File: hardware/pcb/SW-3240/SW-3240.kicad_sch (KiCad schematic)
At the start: 39 parts, among them J1 MIC, J10 CH_D, J2 LINE IN, J3 ESPFlash, J4 JTAG, J5 I2C, J6 FP_IO, J7 CH_A, J8 CH_B, J9 CH_C, SW1 RESET, SW2 BOOT, U1 SW-32MA, U2 MCP4728, U3 ESP32-WROOM-32D, U4 Channel A, U5 Channel B, U6 Channel C, U7 Channel D

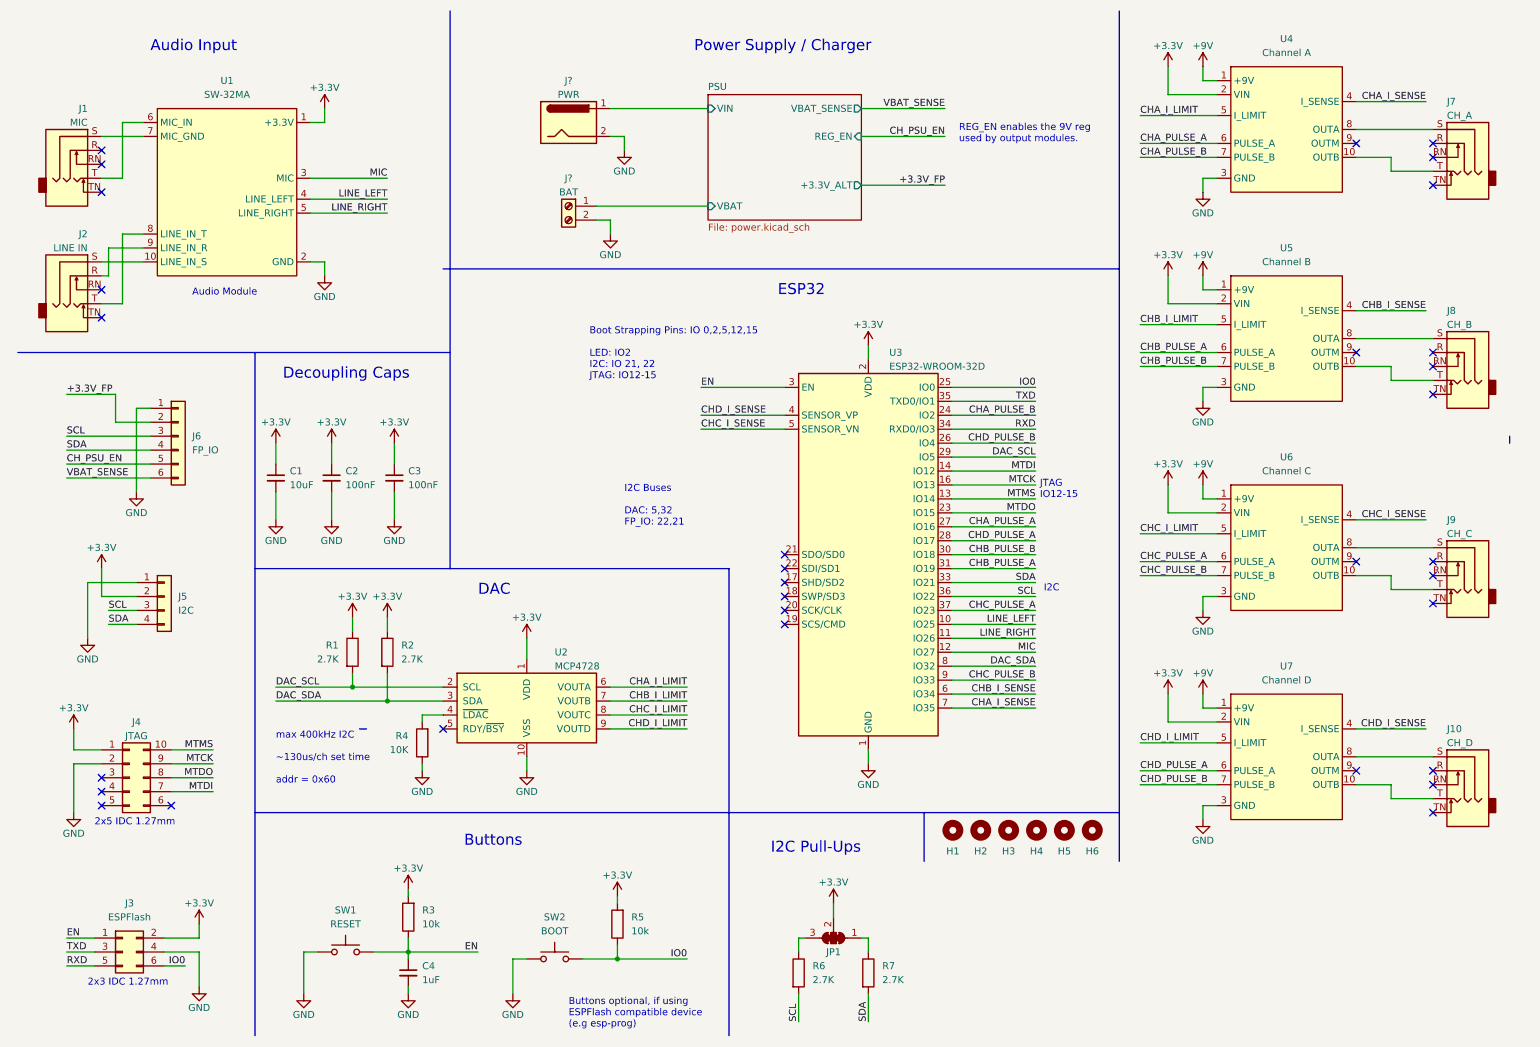
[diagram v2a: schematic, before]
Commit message: fix footprint pin mismatch
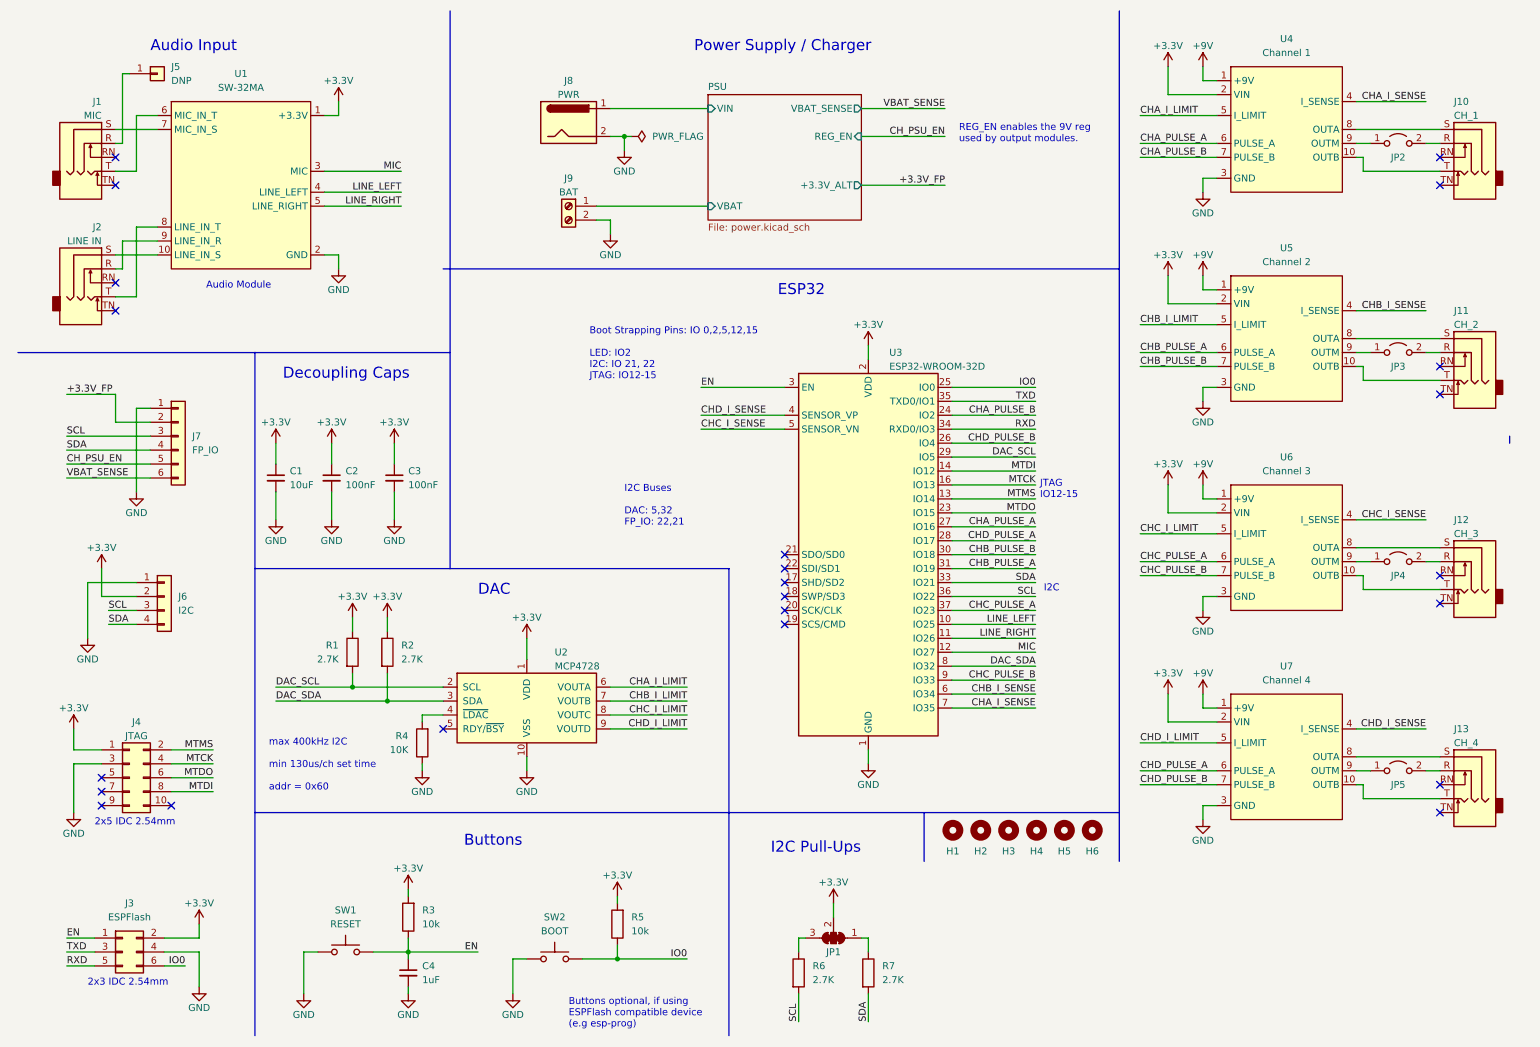
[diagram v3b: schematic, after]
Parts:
- added J5: DNP, Connector_PinHeader_2.54mm:PinHeader_1x01_P2.54mm_Vertical, symbol Connector_Generic:Conn_01x01
- added JP2, JP3, JP4, JP5: Jumper_2_Open, Connector_PinHeader_2.54mm:PinHeader_2x01_P2.54mm_Vertical, symbol Jumper:Jumper_2_Open
- J10: renamed from J7; value CH_A -> CH_1
- J11: renamed from J8; value CH_B -> CH_2
- J12: renamed from J9; value CH_C -> CH_3
- J13: renamed from J10; value CH_D -> CH_4
- J3: footprint Connector_PinHeader_1.27mm:PinHeader_2x03_P1.27mm_Vertical -> Connector_PinHeader_2.54mm:PinHeader_2x03_P2.54mm_Vertical
- J4: footprint Connector_PinHeader_1.27mm:PinHeader_2x05_P1.27mm_Vertical -> Connector_PinHeader_2.54mm:PinHeader_2x05_P2.54mm_Vertical; symbol Connector_Generic:Conn_02x05_Counter_Clockwise -> Connector_Generic:Conn_02x05_Odd_Even
- U4: value Channel A -> Channel 1
- U5: value Channel B -> Channel 2
- U6: value Channel C -> Channel 3
- U7: value Channel D -> Channel 4
- gave numbers to parts that had none: 2
- renumbered J5 to J6, J6 to J7
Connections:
- net GND: now also J4.3 (Pin_3); no longer J4.2 (Pin_2)
- net MTCK: now also J4.4 (Pin_4); no longer J4.9 (Pin_9)
- net MTDI: now also J4.8 (Pin_8); no longer J4.7 (Pin_7)
- net MTDO: now also J4.6 (Pin_6); no longer J4.8 (Pin_8)
- net MTMS: now also J4.2 (Pin_2); no longer J4.10 (Pin_10)
- net at J10.R: now also JP2.2 (B)
- net at J11.R: now also JP3.2 (B)
- net at U5.9 (OUTM): now also JP3.1 (A)
- net at J1.R: now also J5.1 (Pin_1)
- net at J12.R: now also JP4.2 (B)
- net at U7.9 (OUTM): now also JP5.1 (A)
- net at J13.R: now also JP5.2 (B)
- net at U6.9 (OUTM): now also JP4.1 (A)
- net at U4.9 (OUTM): now also JP2.1 (A)
- no-connect marks 32 -> 23
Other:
- note added: "2x3 IDC 2.54mm"
- note added: "2x5 IDC 2.54mm"
- note added: "max 400kHz I2C min 130us/ch set time addr = 0x60"
- note removed: "2x3 IDC 1.27mm"
- note removed: "2x5 IDC 1.27mm"
- note removed: "max 400kHz I2C ~130us/ch set time addr = 0x60"
- moved on the sheet: J1, J10, J11, J12, J13, J2, U1

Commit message: many changes
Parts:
- removed SW1: RESET, Button_Switch_SMD:SW_Push_SPST_NO_Alps_SKRK, symbol Switch:SW_Push
- removed SW2: BOOT, Button_Switch_SMD:SW_Push_SPST_NO_Alps_SKRK, symbol Switch:SW_Push
- added C1: 10uF, Capacitor_SMD:C_0603_1608Metric, symbol Device:C_Small
- added C3: 100uF, Capacitor_SMD:C_0603_1608Metric, symbol Device:C_Small
- added J1: AUX_MIC_IN, Connector_PinHeader_2.54mm:PinHeader_1x02_P2.54mm_Vertical, symbol Connector_Generic:Conn_01x02
- added J11: RESET/FLASH, Connector_PinHeader_2.54mm:PinHeader_2x02_P2.54mm_Vertical, symbol Connector_Generic:Conn_02x02_Odd_Even
- added J2: AUX_LINE_IN, Connector_PinHeader_2.54mm:PinHeader_1x04_P2.54mm_Vertical, symbol Connector_Generic:Conn_01x04
- added J7: FP_5V, Connector_JST:JST_XH_B2B-XH-A_1x02_P2.50mm_Vertical, symbol Connector_Generic:Conn_01x02
- J10: renamed from J7; footprint (none) -> Connector_JST:JST_XH_B6B-XH-A_1x06_P2.50mm_Vertical
- J9: renamed from J5; value DNP -> MIC_IN_R
- JP2, JP3, JP4, JP5: value Jumper_2_Open -> TRI_PHASE
- renumbered C1 to C5, C3 to C6, J8 to J12, J9 to J13, J10 to J14, J11 to J15, J12 to J16, J13 to J17, J1 to J3, J2 to J4, J4 to J5, J3 to J6, J6 to J8, R4 to R3, R5 to R4, R3 to R5
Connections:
- net +3V3: now also C1.1, C3.1
- net CHA_PULSE_A: now also U3.26 (IO4); no longer U3.27 (IO16)
- net CHD_PULSE_B: now also U3.27 (IO16); no longer U3.26 (IO4)
- net EN: now also J11.2 (Pin_2)
- net GND: now also C1.2, C3.2, J11.1 (Pin_1), J11.3 (Pin_3), J7.2 (Pin_2)
- net IO0: now also J11.4 (Pin_4)
- net LINE_LEFT: now also U3.11 (IO26); no longer U3.10 (IO25)
- net LINE_RIGHT: now also U3.10 (IO25); no longer U3.11 (IO26)
- net at J3.S, U1.7 (MIC_IN_S): now also J1.1 (Pin_1)
- net at J3.TN: now also J1.2 (Pin_2)
- net at J4.S, U1.10 (LINE_IN_S): now also J2.2 (Pin_2), J2.3 (Pin_3)
- net at J4.RN: now also J2.4 (Pin_4)
- net at J4.TN: now also J2.1 (Pin_1)
- new net +5V: J7.1 (Pin_1)
- no-connect marks 23 -> 20
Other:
- note added: "Boot Strapping Pins (Pull-up/down): - 0 PU - 2 PD - 5 PU - 12 PD - 15 PU Front Panel I2C: IO 21, 22 DAC I2C: IO 32,5 JTAG: IO12-15"
- note added: "DNP"
- note added: "Manual Reset/Boot"
- note added: "Output Channels"
- note added: "Pin header for manually resetting/flashing the ESP-32. Not needed, if using an ESPFlash compatible device (e.g esp-prog)."
- note added: "Separate 1A 3.3V output used for front panel"
- note removed: "Boot Strapping Pins: IO 0,2,5,12,15 LED: IO2 I2C: IO 21, 22 JTAG: IO12-15"
- note removed: "Buttons"
- note removed: "Buttons optional, if using ESPFlash compatible device (e.g esp-prog)"
- note removed: "Decoupling Caps"
- note removed: "I2C Buses DAC: 5,32 FP_IO: 22,21"
- moved on the sheet: C2, C4, C5, C6, J10, J3, J4, J5, J6, J8, J9, R4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

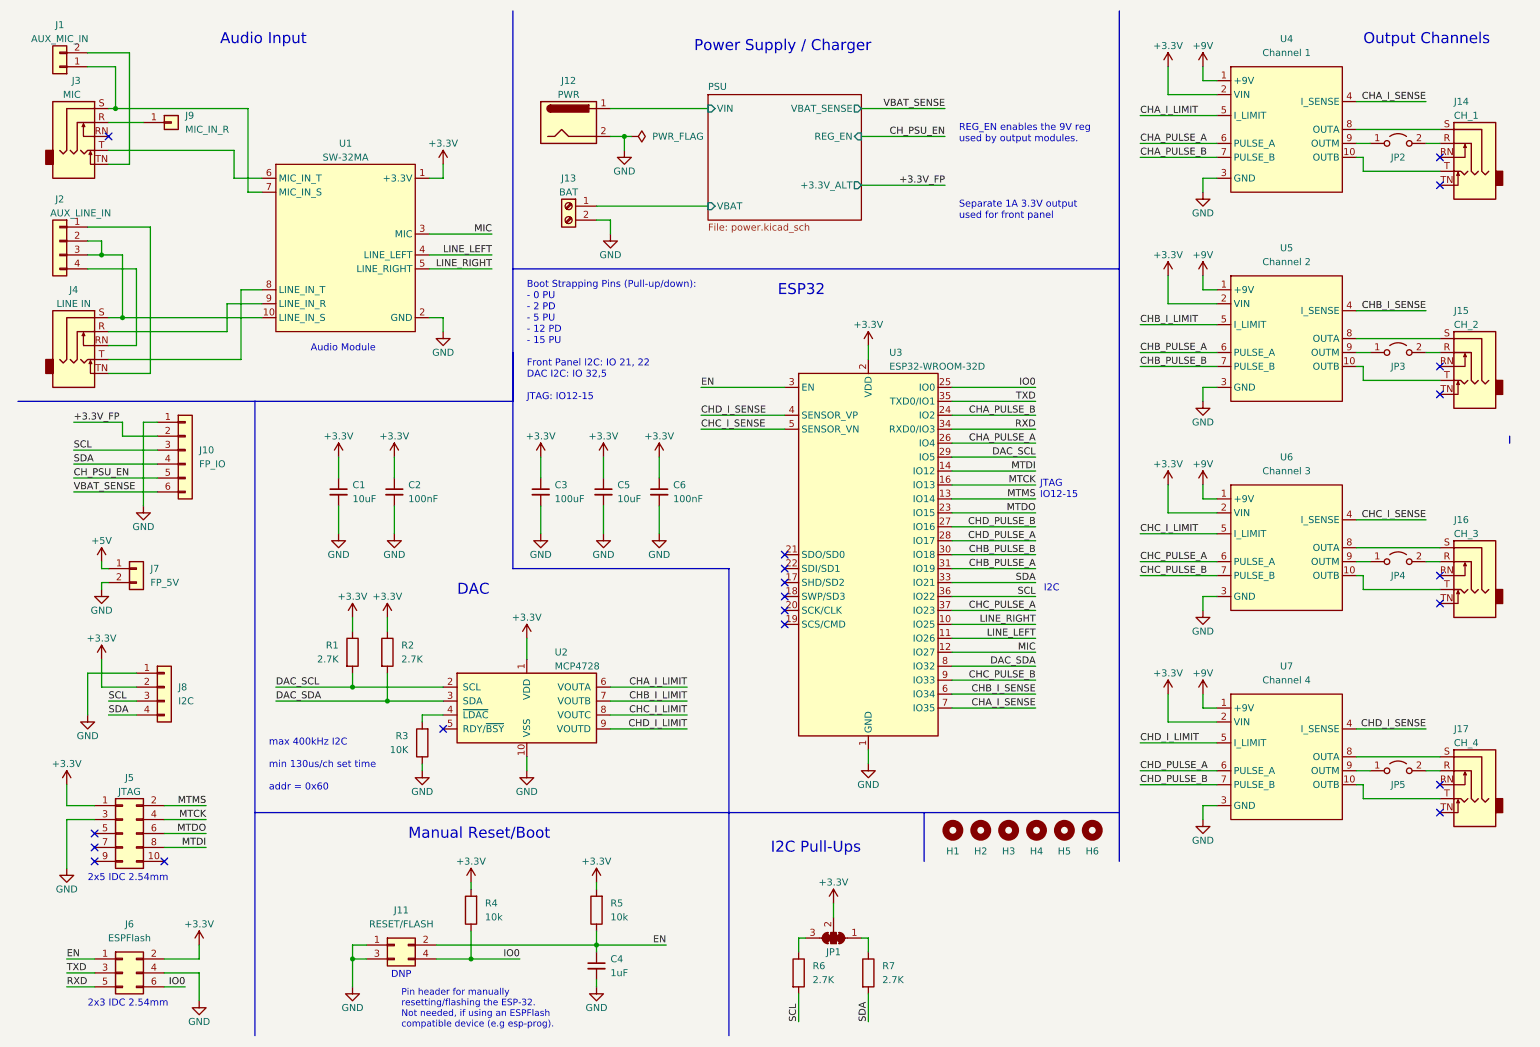
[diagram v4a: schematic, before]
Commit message: use 5v for front panel connector
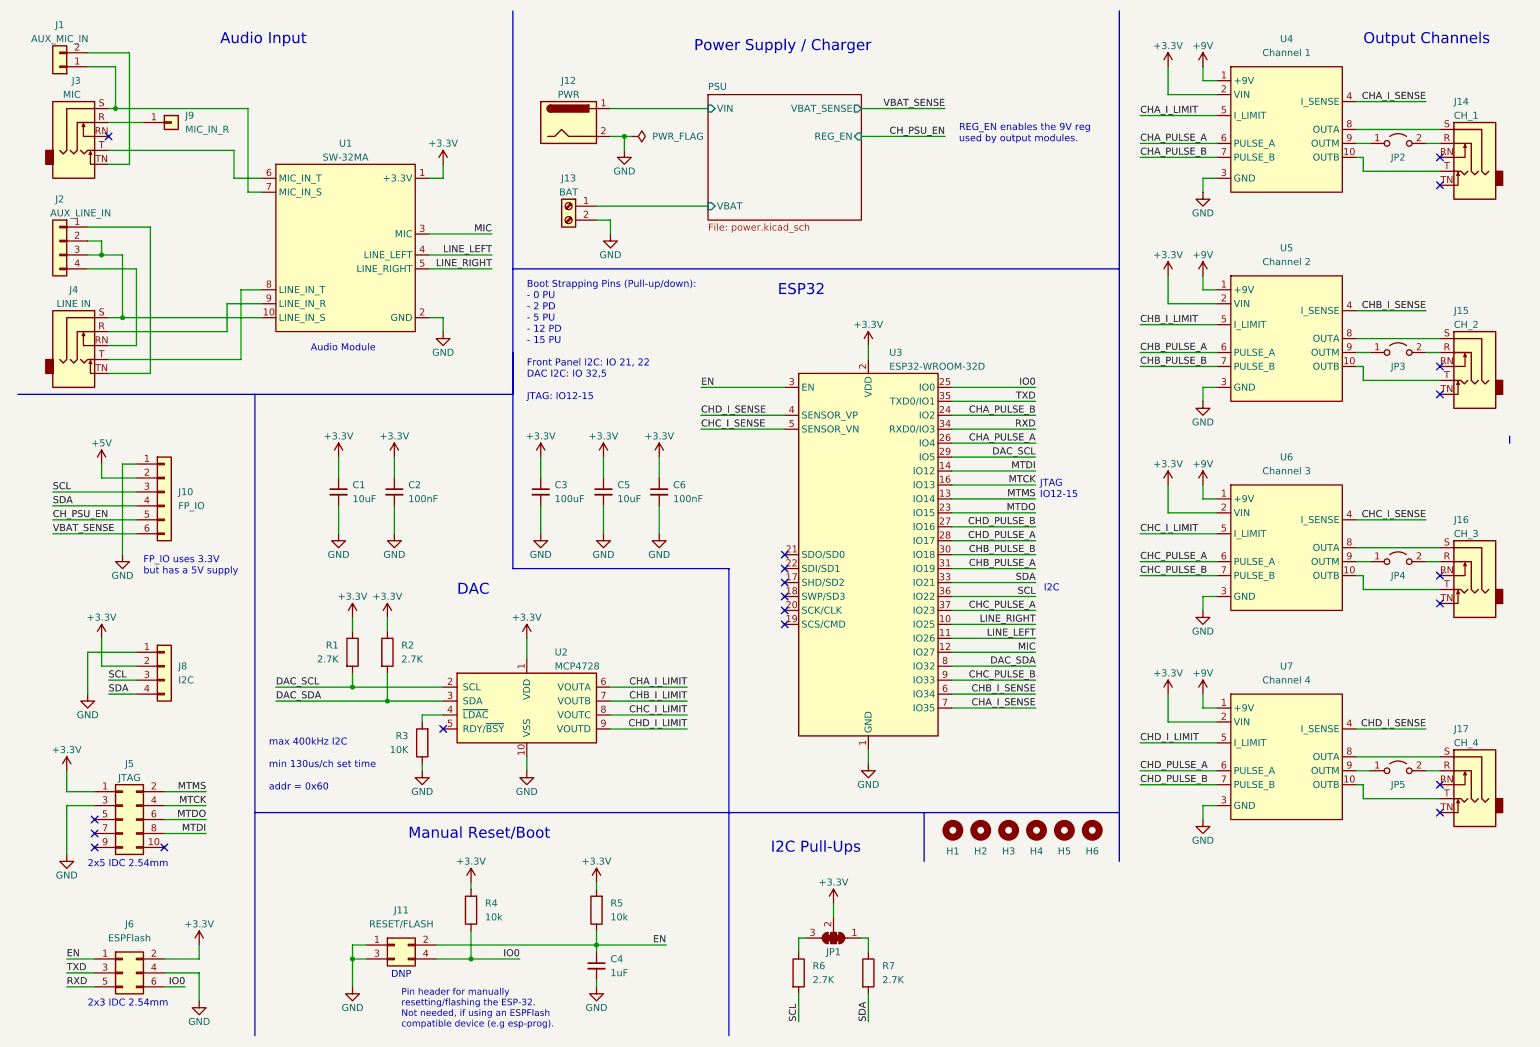
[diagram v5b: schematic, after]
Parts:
- removed J7: FP_5V, Connector_JST:JST_XH_B2B-XH-A_1x02_P2.50mm_Vertical, symbol Connector_Generic:Conn_01x02
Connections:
- net +3.3V_FP is gone; now on net +5V: J10.2 (Pin_2)
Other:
- sheet PSU ports: added none; removed +3.3V_ALT
- note added: "FP_IO uses 3.3V but has a 5V supply"
- note removed: "Separate 1A 3.3V output used for front panel"
- moved on the sheet: J10, J5, J8
